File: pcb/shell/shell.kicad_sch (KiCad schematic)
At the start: 126 parts, among them J1 Conn_01x15, J2 Conn_01x15

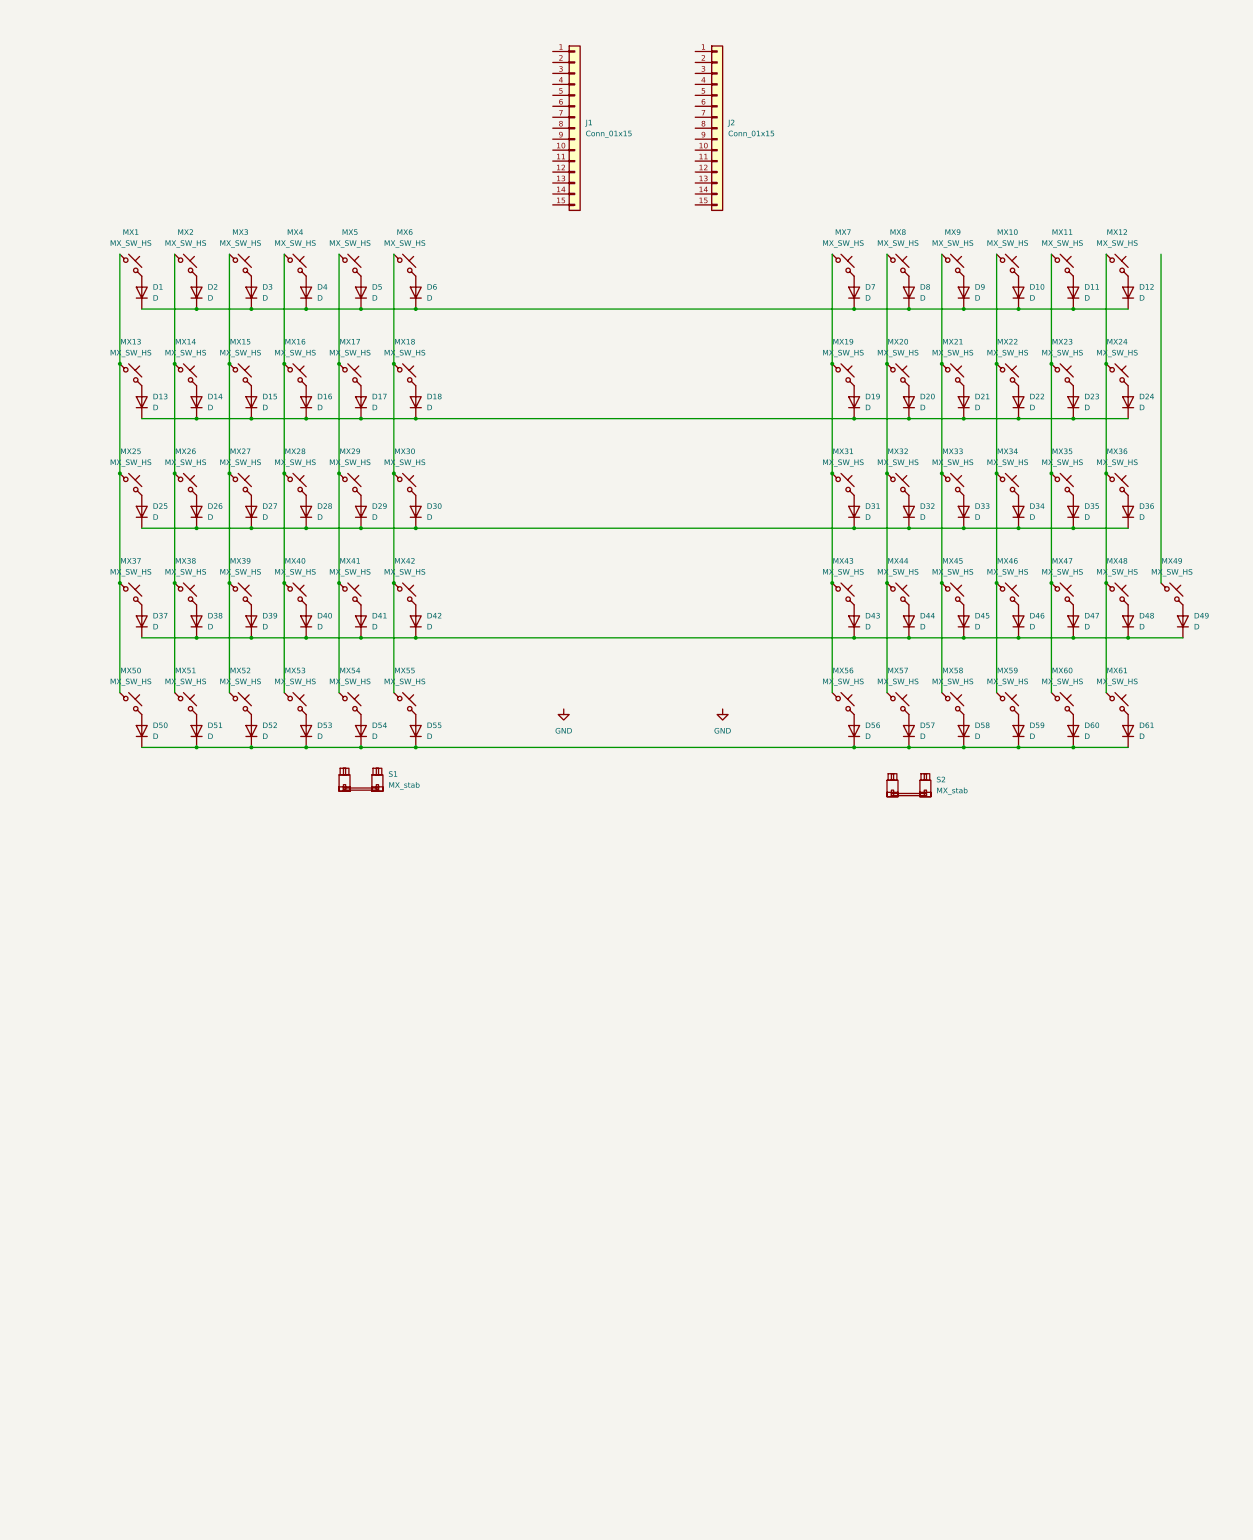
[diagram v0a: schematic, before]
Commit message: updated pcb edge cut
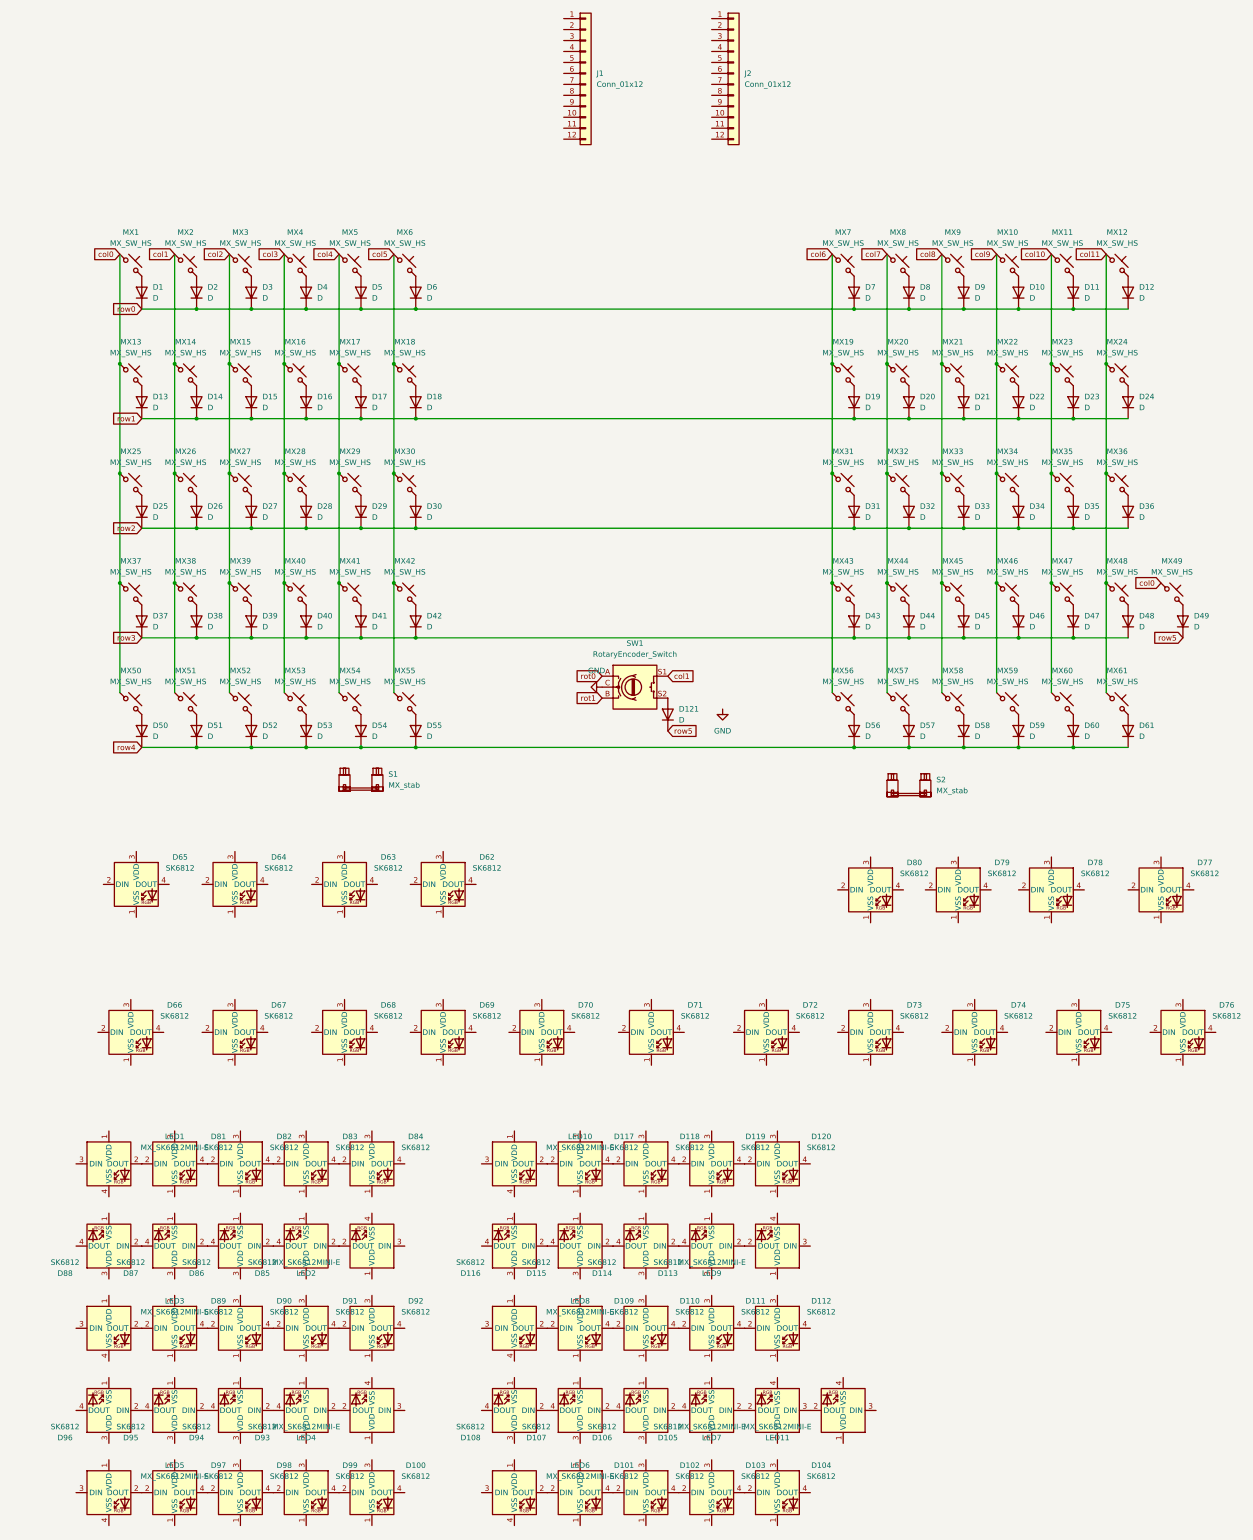
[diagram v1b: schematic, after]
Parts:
- removed J1, J2: Conn_01x15, Connector_PinHeader_2.54mm:PinHeader_1x15_P2.54mm_Vertical, symbol Connector_Generic:Conn_01x15
- added D100, D101, D102, D103, D104, D105, D106, D107, D108, D109, D110, D111, D112, D113, D114, D115, D116, D117, D118, D119, D120, D62, D63, D64, D65, D66, D67, D68, D69, D70, D71, D72, D73, D74, D75, D76, D77, D78, D79, D80, D81, D82, D83, D84, D85, D86, D87, D88, D89, D90, D91, D92, D93, D94, D95, D96, D97, D98, D99: SK6812, LED_SMD:LED_SK6812_PLCC4_5.0x5.0mm_P3.2mm, symbol LED:SK6812
- added D121: D, Diode_SMD:D_SOD-123, symbol Device:D
- added J1, J2: Conn_01x12, symbol Connector_Generic:Conn_01x12
- added LED1, LED10, LED11, LED2, LED3, LED4, LED5, LED6, LED7, LED8, LED9: MX_SK6812MINI-E, PCM_marbastlib-mx:LED_MX_6028R, symbol PCM_marbastlib-mx:MX_SK6812MINI-E
- added SW1: RotaryEncoder_Switch, symbol Device:RotaryEncoder_Switch
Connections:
- net GND: now also SW1.C
- net col5: now reaches MX18.1, MX30.1, MX42.1, MX55.1, MX6.1
- net col11: now reaches MX12.1, MX24.1, MX36.1, MX48.1, MX61.1
- net col7: now reaches MX20.1, MX32.1, MX44.1, MX57.1, MX8.1
- net col4: now reaches MX17.1, MX29.1, MX41.1, MX5.1, MX54.1
- net col2: now reaches MX15.1, MX27.1, MX3.1, MX39.1, MX52.1
- net row0: now reaches D1.1 (K), D10.1 (K), D11.1 (K), D12.1 (K), D2.1 (K), D3.1 (K), D4.1 (K), D5.1 (K), D6.1 (K), D7.1 (K), D8.1 (K), D9.1 (K)
- net row1: now reaches D13.1 (K), D14.1 (K), D15.1 (K), D16.1 (K), D17.1 (K), D18.1 (K), D19.1 (K), D20.1 (K), D21.1 (K), D22.1 (K), D23.1 (K), D24.1 (K)
- net row3: now reaches D37.1 (K), D38.1 (K), D39.1 (K), D40.1 (K), D41.1 (K), D42.1 (K), D43.1 (K), D44.1 (K), D45.1 (K), D46.1 (K), D47.1 (K), D48.1 (K)
- net row3: no longer D49.1 (K)
- net col9: now reaches MX10.1, MX22.1, MX34.1, MX46.1, MX59.1
- net col6: now reaches MX19.1, MX31.1, MX43.1, MX56.1, MX7.1
- net row4: now reaches D50.1 (K), D51.1 (K), D52.1 (K), D53.1 (K), D54.1 (K), D55.1 (K), D56.1 (K), D57.1 (K), D58.1 (K), D59.1 (K), D60.1 (K), D61.1 (K)
- net row2: now reaches D25.1 (K), D26.1 (K), D27.1 (K), D28.1 (K), D29.1 (K), D30.1 (K), D31.1 (K), D32.1 (K), D33.1 (K), D34.1 (K), D35.1 (K), D36.1 (K)
- net col0: now reaches MX1.1, MX13.1, MX25.1, MX37.1, MX50.1
- net col0: now also MX49.1
- net col1: now reaches MX14.1, MX2.1, MX26.1, MX38.1, MX51.1
- net col1: now also SW1.S1
- net col8: now reaches MX21.1, MX33.1, MX45.1, MX58.1, MX9.1
- net col10: now reaches MX11.1, MX23.1, MX35.1, MX47.1, MX60.1
- net col3: now reaches MX16.1, MX28.1, MX4.1, MX40.1, MX53.1
- new net: D90.4 (DOUT), D91.2 (DIN)
- new net: D91.4 (DOUT), D92.2 (DIN)
- new net: D114.4 (DOUT), D115.2 (DIN)
- new net: D115.4 (DOUT), D116.2 (DIN)
- new net: D109.2 (DIN), LED8.2 (DOUT)
- new net: D105.2 (DIN), LED7.2 (DOUT)
- new net: LED11.2 (DOUT), LED7.3 (DIN)
- new net: D81.2 (DIN), LED1.2 (DOUT)
- new net: D81.4 (DOUT), D82.2 (DIN)
- new net: D93.2 (DIN), LED4.2 (DOUT)
- new net: D100.2 (DIN), D99.4 (DOUT)
- new net: D109.4 (DOUT), D110.2 (DIN)
- new net: D110.4 (DOUT), D111.2 (DIN)
- new net: D117.2 (DIN), LED10.2 (DOUT)
- new net: D97.2 (DIN), LED5.2 (DOUT)
- new net: D95.4 (DOUT), D96.2 (DIN)
- new net: D83.4 (DOUT), D84.2 (DIN)
- new net: D102.4 (DOUT), D103.2 (DIN)
- new net: D103.4 (DOUT), D104.2 (DIN)
- new net: D93.4 (DOUT), D94.2 (DIN)
- new net: D94.4 (DOUT), D95.2 (DIN)
- new net: D111.4 (DOUT), D112.2 (DIN)
- new net: D107.4 (DOUT), D108.2 (DIN)
- new net: D121.2 (A), SW1.S2
- new net: D89.4 (DOUT), D90.2 (DIN)
- new net: D86.4 (DOUT), D87.2 (DIN)
- new net: D87.4 (DOUT), D88.2 (DIN)
- new net: D105.4 (DOUT), D106.2 (DIN)
- new net: D97.4 (DOUT), D98.2 (DIN)
- new net: D118.4 (DOUT), D119.2 (DIN)
- new net: D119.4 (DOUT), D120.2 (DIN)
- new net: D117.4 (DOUT), D118.2 (DIN)
- new net: D98.4 (DOUT), D99.2 (DIN)
- new net: D106.4 (DOUT), D107.2 (DIN)
- new net: D85.2 (DIN), LED2.2 (DOUT)
- new net: D89.2 (DIN), LED3.2 (DOUT)
- new net: D113.2 (DIN), LED9.2 (DOUT)
- new net: D113.4 (DOUT), D114.2 (DIN)
- new net: D101.2 (DIN), LED6.2 (DOUT)
- new net: D101.4 (DOUT), D102.2 (DIN)
- new net: D82.4 (DOUT), D83.2 (DIN)
- new net: D85.4 (DOUT), D86.2 (DIN)
- new net rot0: SW1.A
- new net rot1: SW1.B
- new net row5: D121.1 (K), D49.1 (K)

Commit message: fixed per key rgb
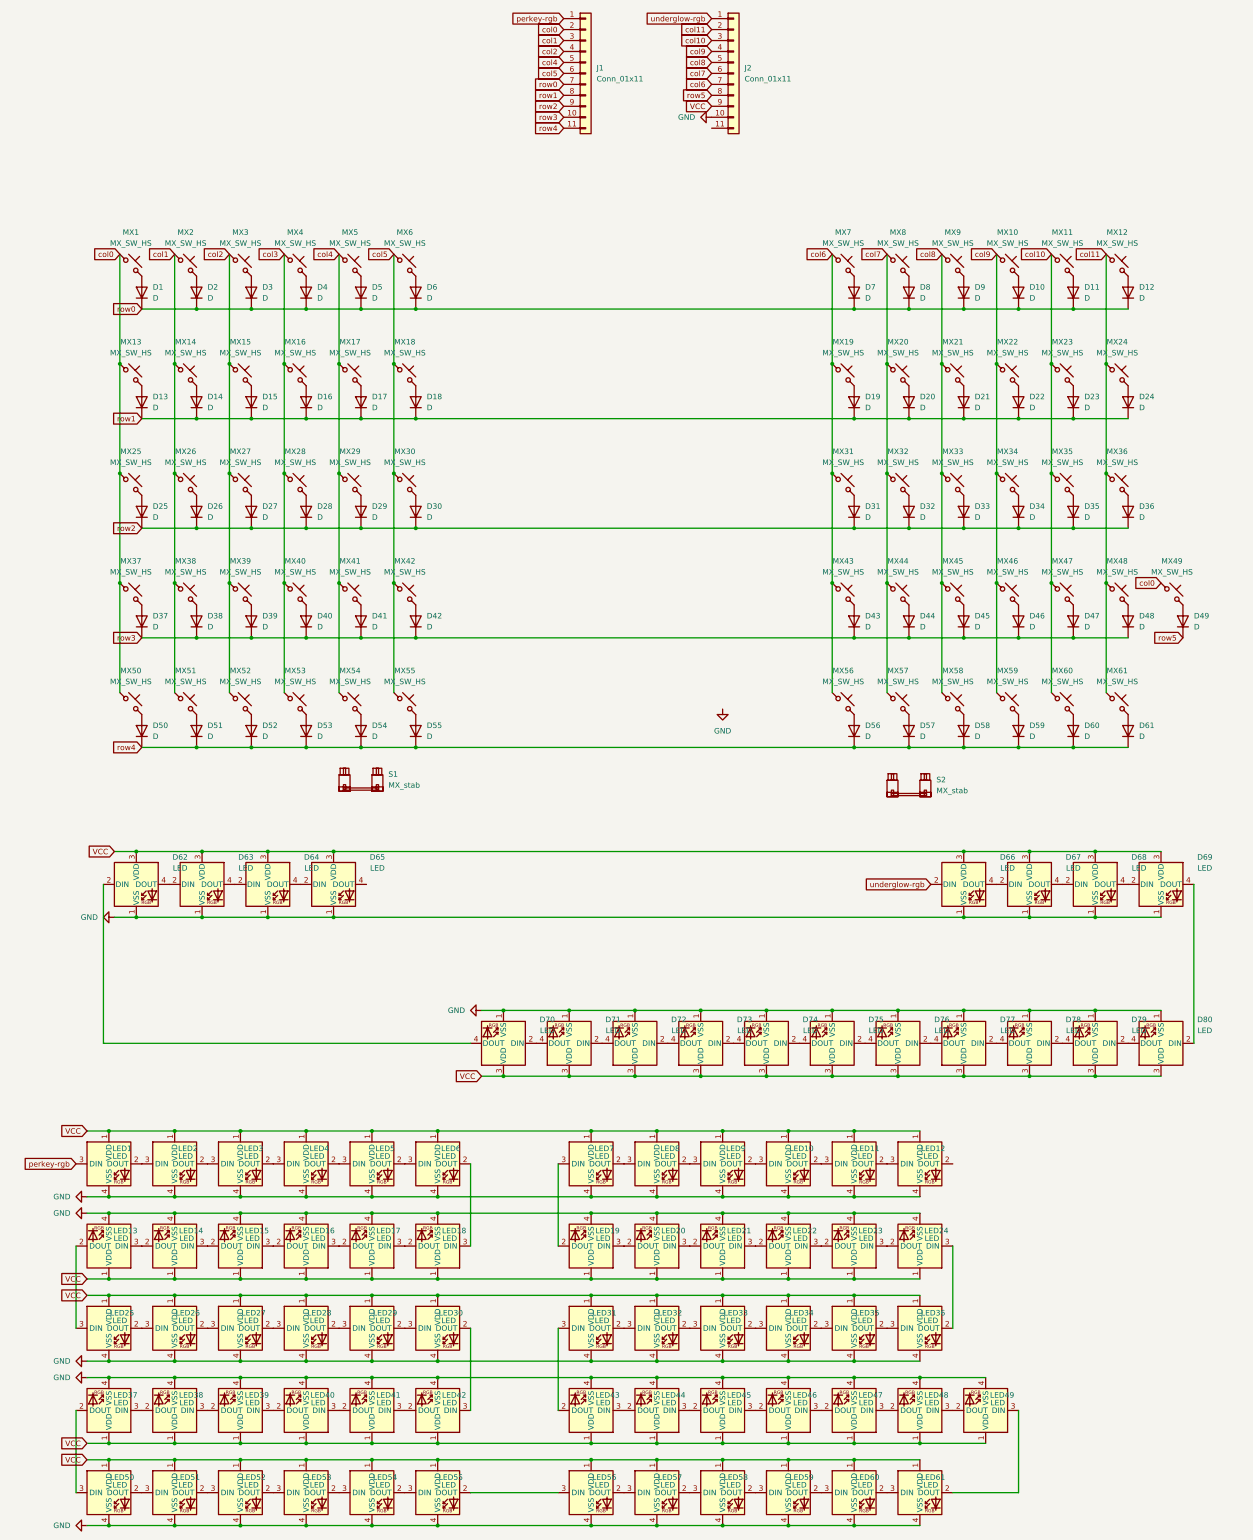
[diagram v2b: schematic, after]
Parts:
- removed D100, D101, D102, D103, D104, D105, D106, D107, D108, D109, D110, D111, D112, D113, D114, D115, D116, D117, D118, D119, D120, D81, D82, D83, D84, D85, D86, D87, D88, D89, D90, D91, D92, D93, D94, D95, D96, D97, D98, D99: SK6812, LED_SMD:LED_SK6812_PLCC4_5.0x5.0mm_P3.2mm, symbol LED:SK6812
- removed D121: D, Diode_SMD:D_SOD-123, symbol Device:D
- removed J1, J2: Conn_01x12, symbol Connector_Generic:Conn_01x12
- removed LED3: MX_SK6812MINI-E, PCM_marbastlib-mx:LED_MX_6028R, symbol PCM_marbastlib-mx:MX_SK6812MINI-E
- removed SW1: RotaryEncoder_Switch, symbol Device:RotaryEncoder_Switch
- added J1, J2: Conn_01x11, Connector_PinSocket_2.54mm:PinSocket_1x11_P2.54mm_Vertical, symbol Connector_Generic:Conn_01x11
- added LED1, LED12, LED25, LED26, LED27, LED28, LED29, LED30, LED31, LED32, LED33, LED34, LED35, LED36, LED50, LED51, LED52, LED53, LED54, LED55, LED56, LED57, LED58, LED59, LED60, LED61: LED, PCM_marbastlib-mx:LED_MX_6028R-ROT, symbol PCM_marbastlib-mx:MX_SK6812MINI-E
- added LED13, LED14, LED15, LED16, LED17, LED18, LED19, LED20, LED21, LED22, LED23, LED24, LED37, LED38, LED39, LED40, LED41, LED42, LED43, LED44, LED45, LED46, LED47, LED48, LED49: LED, PCM_marbastlib-mx:LED_MX_6028R, symbol PCM_marbastlib-mx:MX_SK6812MINI-E
- D62: renamed from D65; value SK6812 -> LED
- D63: renamed from D64; value SK6812 -> LED
- D64: renamed from D63; value SK6812 -> LED
- D65: renamed from D62; value SK6812 -> LED
- D66: renamed from D80; value SK6812 -> LED
- D67: renamed from D79; value SK6812 -> LED
- D68: renamed from D78; value SK6812 -> LED
- D69: renamed from D77; value SK6812 -> LED
- D70: renamed from D66; value SK6812 -> LED
- D71: renamed from D67; value SK6812 -> LED
- D72: renamed from D68; value SK6812 -> LED
- D73: renamed from D69; value SK6812 -> LED
- D74: renamed from D70; value SK6812 -> LED
- D75: renamed from D71; value SK6812 -> LED
- D76: renamed from D72; value SK6812 -> LED
- D77: renamed from D73; value SK6812 -> LED
- D78: renamed from D74; value SK6812 -> LED
- D79: renamed from D75; value SK6812 -> LED
- D80: renamed from D76; value SK6812 -> LED
- LED10, LED11, LED2, LED4, LED5, LED6, LED7, LED8, LED9: value MX_SK6812MINI-E -> LED; footprint PCM_marbastlib-mx:LED_MX_6028R -> PCM_marbastlib-mx:LED_MX_6028R-ROT
- LED3: renamed from LED1; value MX_SK6812MINI-E -> LED; footprint PCM_marbastlib-mx:LED_MX_6028R -> PCM_marbastlib-mx:LED_MX_6028R-ROT
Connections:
- net GND: now also D62.1 (VSS), D63.1 (VSS), D64.1 (VSS), D65.1 (VSS), D66.1 (VSS), D67.1 (VSS), D68.1 (VSS), D69.1 (VSS), D70.1 (VSS), D71.1 (VSS), D72.1 (VSS), D73.1 (VSS), D74.1 (VSS), D75.1 (VSS), D76.1 (VSS), D77.1 (VSS), D78.1 (VSS), D79.1 (VSS), D80.1 (VSS), LED10.4 (VSS), LED11.4 (VSS), LED2.4 (VSS), LED3.4 (VSS), LED4.4 (VSS), LED5.4 (VSS), LED6.4 (VSS), LED7.4 (VSS), LED8.4 (VSS), LED9.4 (VSS), J2.10 (Pin_10), LED1.4 (VSS), LED12.4 (VSS), LED13.4 (VSS), LED14.4 (VSS), LED15.4 (VSS), LED16.4 (VSS), LED17.4 (VSS), LED18.4 (VSS), LED19.4 (VSS), LED20.4 (VSS), LED21.4 (VSS), LED22.4 (VSS), LED23.4 (VSS), LED24.4 (VSS), LED25.4 (VSS), LED26.4 (VSS), LED27.4 (VSS), LED28.4 (VSS), LED29.4 (VSS), LED30.4 (VSS), LED31.4 (VSS), LED32.4 (VSS), LED33.4 (VSS), LED34.4 (VSS), LED35.4 (VSS), LED36.4 (VSS), LED37.4 (VSS), LED38.4 (VSS), LED39.4 (VSS), LED40.4 (VSS), LED41.4 (VSS), LED42.4 (VSS), LED43.4 (VSS), LED44.4 (VSS), LED45.4 (VSS), LED46.4 (VSS), LED47.4 (VSS), LED48.4 (VSS), LED49.4 (VSS), LED50.4 (VSS), LED51.4 (VSS), LED52.4 (VSS), LED53.4 (VSS), LED54.4 (VSS), LED55.4 (VSS), LED56.4 (VSS), LED57.4 (VSS), LED58.4 (VSS), LED59.4 (VSS), LED60.4 (VSS), LED61.4 (VSS)
- net col0: now also J1.2 (Pin_2)
- net col1: now also J1.3 (Pin_3)
- net col10: now also J2.3 (Pin_3)
- net col11: now also J2.2 (Pin_2)
- net col2: now also J1.4 (Pin_4)
- net col4: now also J1.5 (Pin_5)
- net col5: now also J1.6 (Pin_6)
- net col6: now also J2.7 (Pin_7)
- net col7: now also J2.6 (Pin_6)
- net col8: now also J2.5 (Pin_5)
- net col9: now also J2.4 (Pin_4)
- net row0: now also J1.7 (Pin_7)
- net row1: now also J1.8 (Pin_8)
- net row2: now also J1.9 (Pin_9)
- net row3: now also J1.10 (Pin_10)
- net row4: now also J1.11 (Pin_11)
- net row5: now also J2.8 (Pin_8)
- net VCC: now reaches LED8.1 (VDD)
- net VCC: now also D62.3 (VDD), D63.3 (VDD), D64.3 (VDD), D65.3 (VDD), D66.3 (VDD), D67.3 (VDD), D68.3 (VDD), D69.3 (VDD), D70.3 (VDD), D71.3 (VDD), D72.3 (VDD), D73.3 (VDD), D74.3 (VDD), D75.3 (VDD), D76.3 (VDD), D77.3 (VDD), D78.3 (VDD), D79.3 (VDD), D80.3 (VDD), LED10.1 (VDD), LED11.1 (VDD), LED2.1 (VDD), LED3.1 (VDD), LED4.1 (VDD), LED5.1 (VDD), LED6.1 (VDD), LED7.1 (VDD), LED9.1 (VDD), J2.9 (Pin_9), LED1.1 (VDD), LED12.1 (VDD), LED13.1 (VDD), LED14.1 (VDD), LED15.1 (VDD), LED16.1 (VDD), LED17.1 (VDD), LED18.1 (VDD), LED19.1 (VDD), LED20.1 (VDD), LED21.1 (VDD), LED22.1 (VDD), LED23.1 (VDD), LED24.1 (VDD), LED25.1 (VDD), LED26.1 (VDD), LED27.1 (VDD), LED28.1 (VDD), LED29.1 (VDD), LED30.1 (VDD), LED31.1 (VDD), LED32.1 (VDD), LED33.1 (VDD), LED34.1 (VDD), LED35.1 (VDD), LED36.1 (VDD), LED37.1 (VDD), LED38.1 (VDD), LED39.1 (VDD), LED40.1 (VDD), LED41.1 (VDD), LED42.1 (VDD), LED43.1 (VDD), LED44.1 (VDD), LED45.1 (VDD), LED46.1 (VDD), LED47.1 (VDD), LED48.1 (VDD), LED49.1 (VDD), LED50.1 (VDD), LED51.1 (VDD), LED52.1 (VDD), LED53.1 (VDD), LED54.1 (VDD), LED55.1 (VDD), LED56.1 (VDD), LED57.1 (VDD), LED58.1 (VDD), LED59.1 (VDD), LED60.1 (VDD), LED61.1 (VDD)
- net at LED8.2 (DOUT): now also LED9.3 (DIN)
- net at LED8.3 (DIN): now also LED7.2 (DOUT)
- net at LED7.3 (DIN): now also LED19.2 (DOUT); no longer LED11.2 (DOUT)
- net at LED3.2 (DOUT): now also LED4.3 (DIN)
- net at LED4.2 (DOUT): now also LED5.3 (DIN)
- net at D69.2 (DIN): now also D68.4 (DOUT)
- net at D69.4 (DOUT): now also D80.2 (DIN)
- net at D64.2 (DIN): now also D63.4 (DOUT)
- net at D64.4 (DOUT): now also D65.2 (DIN)
- net at D78.2 (DIN): now also D79.4 (DOUT)
- net at D78.4 (DOUT): now also D77.2 (DIN)
- net at LED10.2 (DOUT): now also LED11.3 (DIN)
- net at LED10.3 (DIN): now also LED9.2 (DOUT)
- net at LED5.2 (DOUT): now also LED6.3 (DIN)
- net at D73.2 (DIN): now also D74.4 (DOUT)
- net at D73.4 (DOUT): now also D72.2 (DIN)
- net at D80.4 (DOUT): now also D79.2 (DIN)
- net at D76.2 (DIN): now also D77.4 (DOUT)
- net at D76.4 (DOUT): now also D75.2 (DIN)
- net at D62.2 (DIN): now also D70.4 (DOUT)
- net at D62.4 (DOUT): now also D63.2 (DIN)
- net at D70.2 (DIN): now also D71.4 (DOUT)
- net at D71.2 (DIN): now also D72.4 (DOUT)
- net at LED2.2 (DOUT): now also LED3.3 (DIN)
- net at LED2.3 (DIN): now also LED1.2 (DOUT)
- net at D74.2 (DIN): now also D75.4 (DOUT)
- net at LED6.2 (DOUT): now also LED18.3 (DIN)
- net at D67.2 (DIN): now also D66.4 (DOUT)
- net at D67.4 (DOUT): now also D68.2 (DIN)
- net underglow-rgb: now reaches D66.2 (DIN)
- net underglow-rgb: now also J2.1 (Pin_1)
- new net: LED46.3 (DIN), LED47.2 (DOUT)
- new net: LED47.3 (DIN), LED48.2 (DOUT)
- new net: LED13.3 (DIN), LED14.2 (DOUT)
- new net: LED14.3 (DIN), LED15.2 (DOUT)
- new net: LED58.2 (DOUT), LED59.3 (DIN)
- new net: LED57.2 (DOUT), LED58.3 (DIN)
- new net: LED55.2 (DOUT), LED56.3 (DIN)
- new net: LED54.2 (DOUT), LED55.3 (DIN)
- new net: LED21.3 (DIN), LED22.2 (DOUT)
- new net: LED22.3 (DIN), LED23.2 (DOUT)
- new net: LED20.3 (DIN), LED21.2 (DOUT)
- new net: LED23.3 (DIN), LED24.2 (DOUT)
- new net: LED15.3 (DIN), LED16.2 (DOUT)
- new net: LED16.3 (DIN), LED17.2 (DOUT)
- new net: LED37.3 (DIN), LED38.2 (DOUT)
- new net: LED38.3 (DIN), LED39.2 (DOUT)
- new net: LED31.2 (DOUT), LED32.3 (DIN)
- new net: LED31.3 (DIN), LED43.2 (DOUT)
- new net: LED25.2 (DOUT), LED26.3 (DIN)
- new net: LED13.2 (DOUT), LED25.3 (DIN)
- new net: LED19.3 (DIN), LED20.2 (DOUT)
- new net: LED50.2 (DOUT), LED51.3 (DIN)
- new net: LED37.2 (DOUT), LED50.3 (DIN)
- new net: LED45.3 (DIN), LED46.2 (DOUT)
- new net: LED11.2 (DOUT), LED12.3 (DIN)
- new net: LED41.3 (DIN), LED42.2 (DOUT)
- new net: LED30.2 (DOUT), LED42.3 (DIN)
- new net: LED56.2 (DOUT), LED57.3 (DIN)
- new net: LED35.2 (DOUT), LED36.3 (DIN)
- new net: LED34.2 (DOUT), LED35.3 (DIN)
- new net: LED24.3 (DIN), LED36.2 (DOUT)
- new net: LED29.2 (DOUT), LED30.3 (DIN)
- new net: LED28.2 (DOUT), LED29.3 (DIN)
- new net: LED27.2 (DOUT), LED28.3 (DIN)
- new net: LED26.2 (DOUT), LED27.3 (DIN)
- new net: LED43.3 (DIN), LED44.2 (DOUT)
- new net: LED48.3 (DIN), LED49.2 (DOUT)
- new net: LED49.3 (DIN), LED61.2 (DOUT)
- new net: LED44.3 (DIN), LED45.2 (DOUT)
- new net: LED32.2 (DOUT), LED33.3 (DIN)
- new net: LED33.2 (DOUT), LED34.3 (DIN)
- new net: LED51.2 (DOUT), LED52.3 (DIN)
- new net: LED60.2 (DOUT), LED61.3 (DIN)
- new net: LED59.2 (DOUT), LED60.3 (DIN)
- new net: LED53.2 (DOUT), LED54.3 (DIN)
- new net: LED52.2 (DOUT), LED53.3 (DIN)
- new net: LED39.3 (DIN), LED40.2 (DOUT)
- new net: LED17.3 (DIN), LED18.2 (DOUT)
- new net: LED40.3 (DIN), LED41.2 (DOUT)
- new net perkey-rgb: J1.1 (Pin_1), LED1.3 (DIN)
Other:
- company: (none) -> floookay
- title: (none) -> barnacle
- moved on the sheet: D63, D64, D65, D66, D67, D68, D69, D70, D71, D72, D73, D74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
